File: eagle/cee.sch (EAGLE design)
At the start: 53 parts, among them IC1 IC1, J1 SOLDERJUMPERNC2

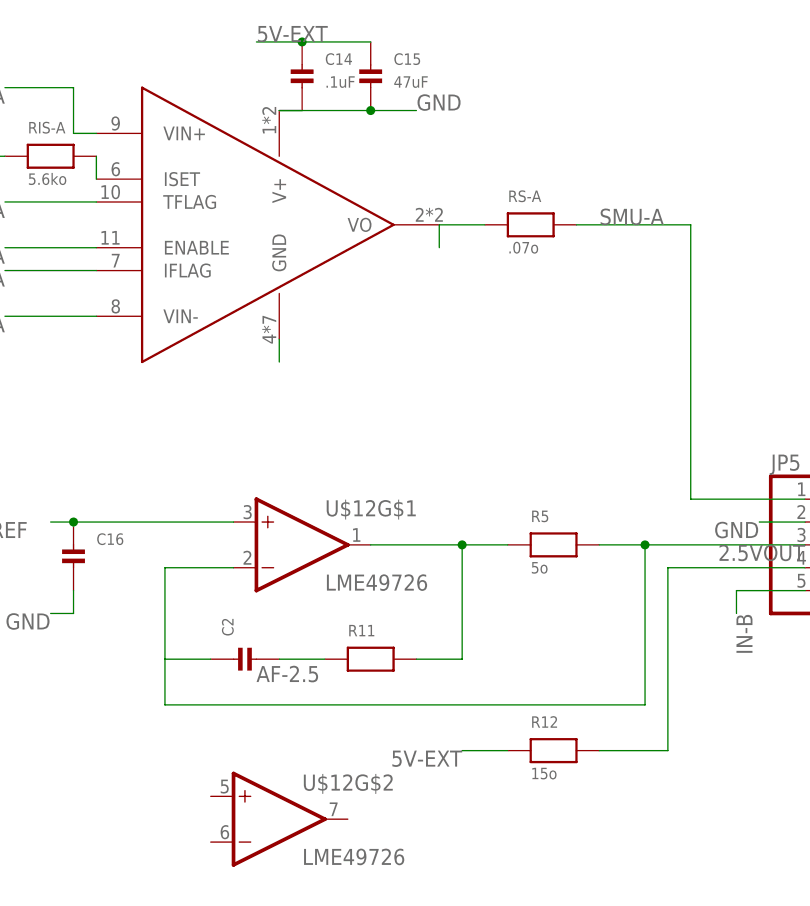
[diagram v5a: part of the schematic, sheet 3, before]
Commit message: Clean up MCP6N11 routing   * Move it to the right place   * Fix 2.5V bypassing   * Fix OPA567 power
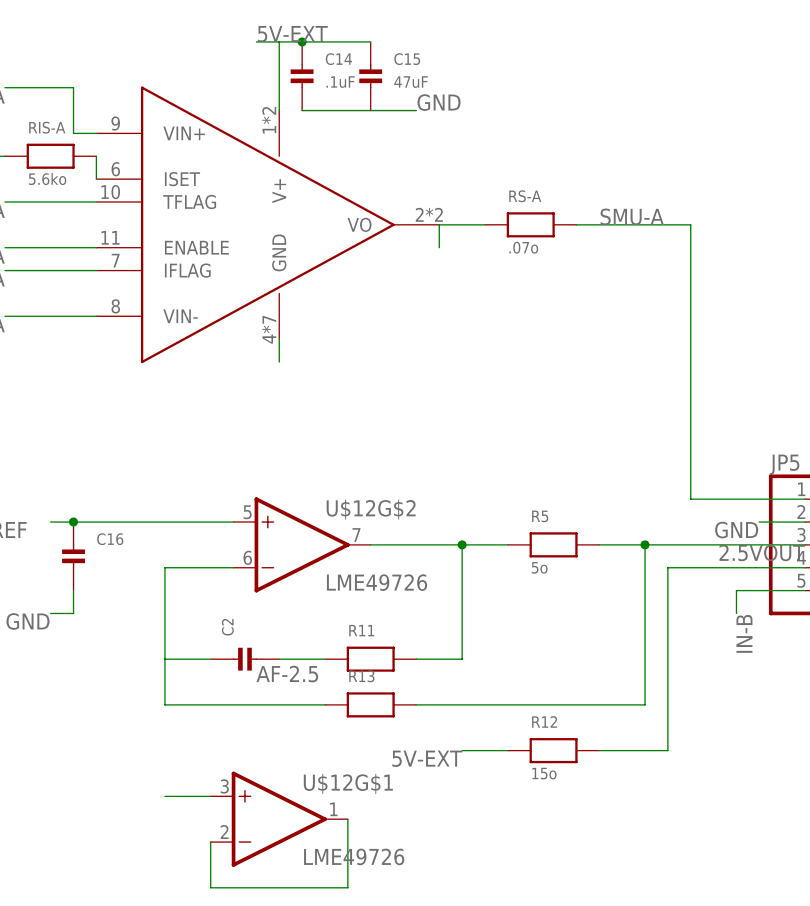
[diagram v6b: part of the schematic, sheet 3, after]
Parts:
- added R13: (no value), nonolith:RESISTOR0603
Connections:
- new net N$13: C2.P$1, R13.1, U$12G$2.-IN
- new net N$15: U$12G$1.-IN, U$12G$1.OUT
- net 2.5VFDBK: now also U$12G$2.OUT; no longer U$12G$1.OUT
- net 2.5VOUT: now also R13.2, U$12G$1.+IN; no longer C2.P$1, U$12G$1.-IN
- net 2.5VREF: now also U$12G$2.+IN; no longer U$12G$1.+IN
- net 5V-EXT: now also OPA-A.V+
- net GND: no longer OPA-A.V+
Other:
- moved on the sheet: U$12G$1, U$12G$2
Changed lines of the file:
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@@
 <?xml version="1.0" encoding="utf-8"?>
 <!DOCTYPE eagle SYSTEM "eagle.dtd">
-<eagle version="6.3">
+<eagle version="6.1">
 <drawing>
 <settings>
@@
 <part name="C2" library="nonolith" deviceset="CAP_CERAMIC" device="0603"/>
 <part name="R12" library="nonolith" deviceset="RESISTOR" device="1206" value="15o"/>
+<part name="R13" library="nonolith" deviceset="RESISTOR" device="0603"/>
 </parts>
 <sheets>
@@
 <instance part="R5" gate="G$1" x="170.18" y="60.96"/>
 <instance part="C12" gate="G$1" x="35.56" y="88.9" rot="R90"/>
-<instance part="U$12" gate="G$1" x="142.24" y="60.96"/>
-<instance part="U$12" gate="G$2" x="139.7" y="30.48"/>
+<instance part="U$12" gate="G$2" x="142.24" y="60.96"/>
+<instance part="U$12" gate="G$1" x="139.7" y="30.48"/>
 <instance part="U$12" gate="G$3" x="106.68" y="38.1"/>
 <instance part="C3" gate="G$1" x="91.44" y="35.56"/>
@@
 <instance part="C2" gate="G$1" x="137.16" y="48.26" rot="R90"/>
 <instance part="R12" gate="G$1" x="170.18" y="38.1"/>
+<instance part="R13" gate="G$1" x="149.86" y="43.18"/>
 </instances>
 <busses>
@@
 </segment>
 <segment>
-<wire x1="139.7" y1="109.22" x2="149.86" y2="109.22" width="0.254" layer="91"/>
 <wire x1="149.86" y1="109.22" x2="154.94" y2="109.22" width="0.254" layer="91"/>
-<junction x="149.86" y="109.22"/>
 <label x="154.94" y="109.22" size="1.778" layer="95"/>
+<pinref part="C15" gate="G$1" pin="P$2"/>
 <pinref part="C14" gate="G$1" pin="P$2"/>
-<pinref part="C15" gate="G$1" pin="P$2"/>
-<pinref part="OPA-A" gate="G$1" pin="V+"/>
-<wire x1="139.7" y1="109.22" x2="142.24" y2="109.22" width="0.1524" layer="91"/>
+<wire x1="142.24" y1="109.22" x2="149.86" y2="109.22" width="0.254" layer="91"/>
 </segment>
 <segment>
@@
 <net name="5V-EXT" class="0">
 <segment>
-<wire x1="137.16" y1="116.84" x2="142.24" y2="116.84" width="0.254" layer="91"/>
+<wire x1="137.16" y1="116.84" x2="139.7" y2="116.84" width="0.254" layer="91"/>
+<wire x1="139.7" y1="116.84" x2="142.24" y2="116.84" width="0.254" layer="91"/>
 <wire x1="142.24" y1="116.84" x2="149.86" y2="116.84" width="0.254" layer="91"/>
 <junction x="142.24" y="116.84"/>
@@
 <pinref part="C14" gate="G$1" pin="P$1"/>
 <pinref part="C15" gate="G$1" pin="P$1"/>
+<pinref part="OPA-A" gate="G$1" pin="V+"/>
+<wire x1="139.7" y1="116.84" x2="139.7" y2="109.22" width="0.254" layer="91"/>
 </segment>
 <segment>
@@
 <net name="2.5VOUT" class="0">
 <segment>
-<pinref part="U$12" gate="G$1" pin="-IN"/>
-<wire x1="134.62" y1="58.42" x2="127" y2="58.42" width="0.254" layer="91"/>
-<wire x1="127" y1="58.42" x2="127" y2="48.26" width="0.254" layer="91"/>
-<wire x1="127" y1="48.26" x2="127" y2="43.18" width="0.254" layer="91"/>
-<wire x1="127" y1="43.18" x2="180.34" y2="43.18" width="0.254" layer="91"/>
+<wire x1="154.94" y1="43.18" x2="180.34" y2="43.18" width="0.254" layer="91"/>
 <wire x1="180.34" y1="43.18" x2="180.34" y2="60.96" width="0.254" layer="91"/>
 <pinref part="R5" gate="G$1" pin="2"/>
@@
 <wire x1="175.26" y1="60.96" x2="180.34" y2="60.96" width="0.254" layer="91"/>
 <label x="198.12" y="60.96" size="1.778" layer="95" rot="R180"/>
-<pinref part="C2" gate="G$1" pin="P$1"/>
 <wire x1="180.34" y1="60.96" x2="198.12" y2="60.96" width="0.254" layer="91"/>
-<wire x1="132.08" y1="48.26" x2="127" y2="48.26" width="0.254" layer="91"/>
 <junction x="180.34" y="60.96"/>
+<pinref part="R13" gate="G$1" pin="2"/>
+</segment>
+<segment>
+<pinref part="U$12" gate="G$1" pin="+IN"/>
+<wire x1="132.08" y1="33.02" x2="127" y2="33.02" width="0.254" layer="91"/>
 </segment>
 </net>
 <net name="2.5VFDBK" class="0">
 <segment>
-<pinref part="U$12" gate="G$1" pin="OUT"/>
+<pinref part="U$12" gate="G$2" pin="OUT"/>
 <wire x1="165.1" y1="60.96" x2="160.02" y2="60.96" width="0.254" layer="91"/>
 <wire x1="160.02" y1="60.96" x2="149.86" y2="60.96" width="0.254" layer="91"/>
@@
 <net name="2.5VREF" class="0">
 <segment>
-<pinref part="U$12" gate="G$1" pin="+IN"/>
+<pinref part="U$12" gate="G$2" pin="+IN"/>
 <wire x1="134.62" y1="63.5" x2="116.84" y2="63.5" width="0.254" layer="91"/>
 <label x="111.76" y="63.5" size="1.778" layer="95" rot="R180"/>
@@
 </segment>
 </net>
+<net name="N$13" class="0">
+<segment>
+<pinref part="R13" gate="G$1" pin="1"/>
+<pinref part="U$12" gate="G$2" pin="-IN"/>
+<wire x1="134.62" y1="58.42" x2="127" y2="58.42" width="0.254" layer="91"/>
+<wire x1="127" y1="58.42" x2="127" y2="48.26" width="0.254" layer="91"/>
+<pinref part="C2" gate="G$1" pin="P$1"/>
+<wire x1="132.08" y1="48.26" x2="127" y2="48.26" width="0.254" layer="91"/>
+<wire x1="127" y1="48.26" x2="127" y2="43.18" width="0.254" layer="91"/>
+<wire x1="127" y1="43.18" x2="144.78" y2="43.18" width="0.254" layer="91"/>
+</segment>
+</net>
+<net name="N$15" class="0">
+<segment>
+<pinref part="U$12" gate="G$1" pin="OUT"/>
+<wire x1="147.32" y1="30.48" x2="147.32" y2="22.86" width="0.254" layer="91"/>
+<pinref part="U$12" gate="G$1" pin="-IN"/>
+<wire x1="147.32" y1="22.86" x2="132.08" y2="22.86" width="0.254" layer="91"/>
+<wire x1="132.08" y1="22.86" x2="132.08" y2="27.94" width="0.254" layer="91"/>
+</segment>
+</net>

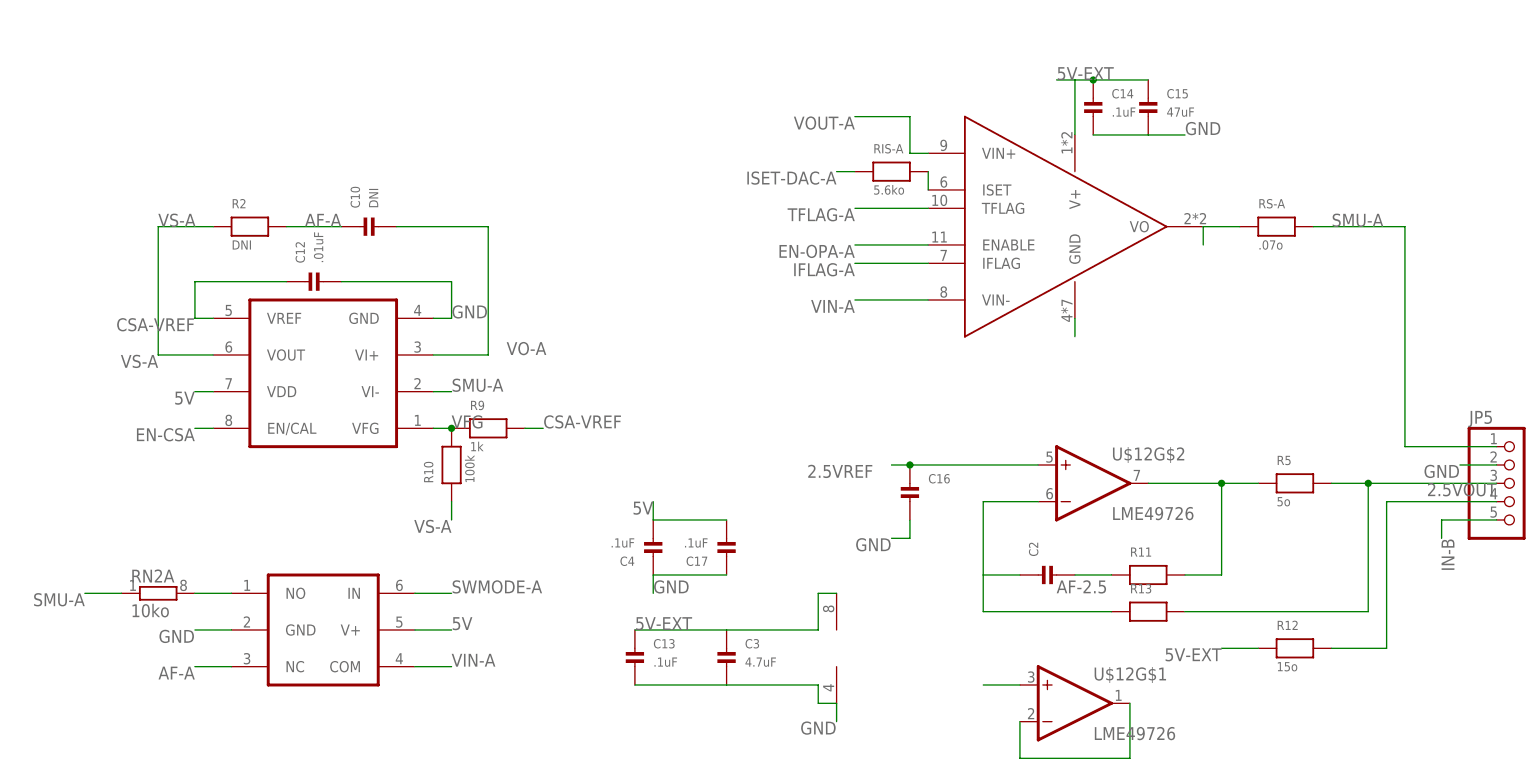
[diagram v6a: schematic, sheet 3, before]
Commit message: Divided 2.5V to ADC gainneg
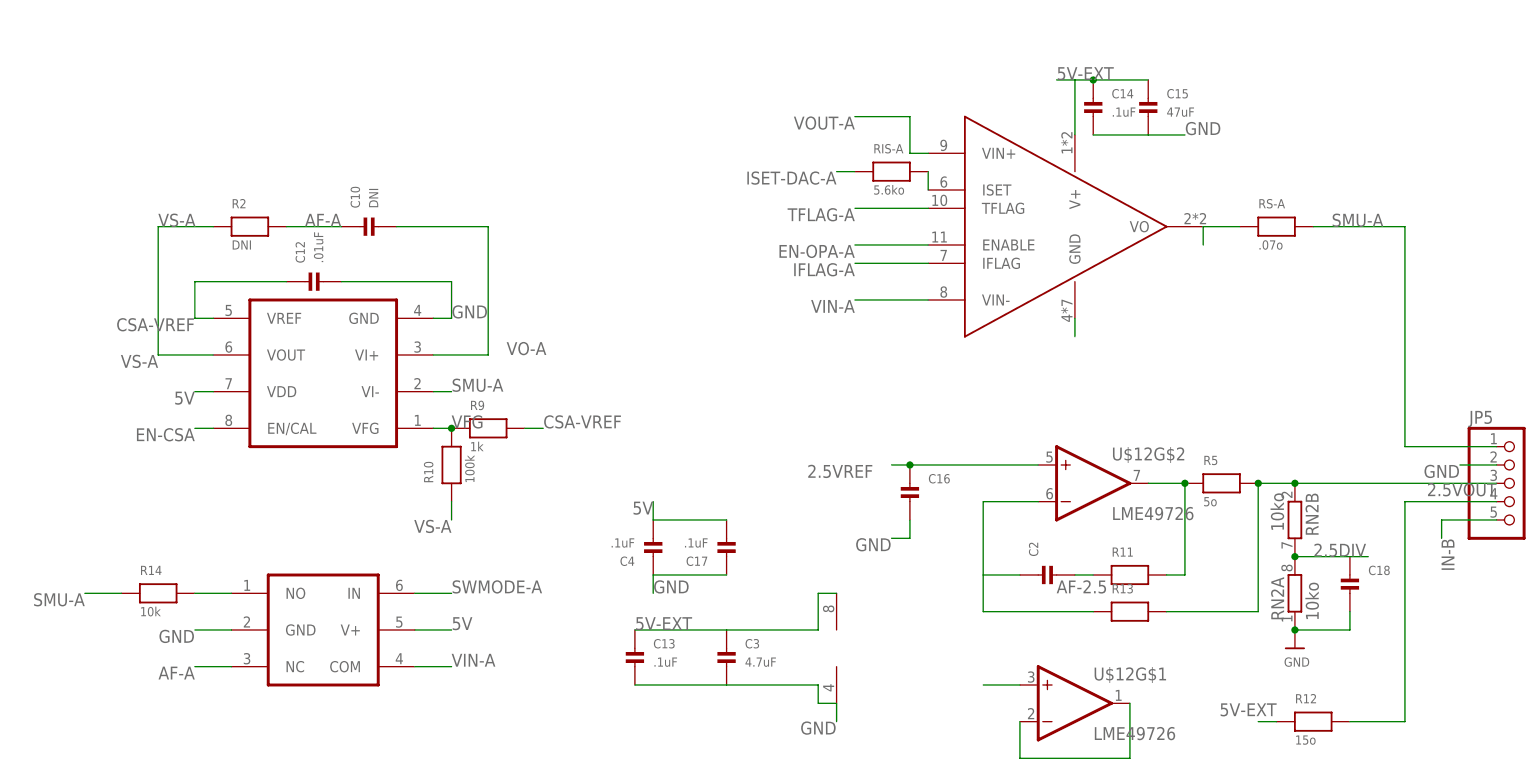
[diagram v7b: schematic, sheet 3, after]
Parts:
- added C18: (no value), nonolith:CAP_CERAMIC0603
- added R14: 10k, nonolith:RESISTOR0603
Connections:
- new net 2.5DIV: C18.P$1, IC1.PA5/ADC5, RN2A.2, RN2B.2
- net 2.5VOUT: now also RN2B.1
- net GND: now also C18.P$2, RN2A.1
- net IN-B: now also RN2D.1; no longer RN2C.1
- net SMU-A: now also R14.1, RN2C.1; no longer RN2A.1, RN2B.1
- net SMUP-A: now also RN2C.2; no longer RN2B.2
- net SMUP-B: now also RN2D.2; no longer RN2C.2
- net SMUP-SW-A: now also R14.2; no longer RN2A.2
- net VOUT-B: now also IC1.PA7/ADC7; no longer IC1.PA5/ADC5
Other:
- moved on the sheet: R11, R12, R13, R5, RN2A, RN2C
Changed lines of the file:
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@@
 <part name="R12" library="nonolith" deviceset="RESISTOR" device="1206" value="15o"/>
 <part name="R13" library="nonolith" deviceset="RESISTOR" device="0603"/>
+<part name="R14" library="nonolith" deviceset="RESISTOR" device="0603" value="10k"/>
+<part name="U$14" library="nonolith" deviceset="GND" device=""/>
+<part name="C18" library="nonolith" deviceset="CAP_CERAMIC" device="0603"/>
 </parts>
 <sheets>
@@
 </segment>
 <segment>
-<wire x1="96.52" y1="17.78" x2="101.6" y2="17.78" width="0.254" layer="91"/>
 <wire x1="96.52" y1="12.7" x2="101.6" y2="12.7" width="0.254" layer="91"/>
-<label x="101.6" y="17.78" size="1.778" layer="95"/>
 <label x="101.6" y="12.7" size="1.778" layer="95"/>
-<pinref part="IC1" gate="G$1" pin="PA5/ADC5"/>
 <pinref part="IC1" gate="G$1" pin="PA3/ADC3"/>
+</segment>
+<segment>
+<pinref part="IC1" gate="G$1" pin="PA7/ADC7"/>
+<wire x1="96.52" y1="22.86" x2="101.6" y2="22.86" width="0.254" layer="91"/>
+<label x="101.6" y="22.86" size="1.778" layer="95"/>
 </segment>
 </net>
@@
 <wire x1="203.2" y1="53.34" x2="195.58" y2="53.34" width="0.254" layer="91"/>
 <label x="195.58" y="53.34" size="1.778" layer="95" rot="R180"/>
+</segment>
+</net>
+<net name="2.5DIV" class="0">
+<segment>
+<pinref part="IC1" gate="G$1" pin="PA5/ADC5"/>
+<wire x1="96.52" y1="17.78" x2="101.6" y2="17.78" width="0.254" layer="91"/>
+<label x="101.6" y="17.78" size="1.778" layer="95"/>
 </segment>
 </net>
@@
 </instance>
 <instance part="OPA-C" gate="G$1" x="22.86" y="58.42" rot="R270"/>
-<instance part="RN2" gate="B" x="5.08" y="45.72" rot="R90"/>
-<instance part="RN2" gate="C" x="5.08" y="17.78" rot="R90"/>
+<instance part="RN2" gate="C" x="5.08" y="45.72" rot="R90"/>
+<instance part="RN2" gate="D" x="5.08" y="17.78" rot="R90"/>
 <instance part="R7" gate="G$1" x="5.08" y="5.08" rot="R90"/>
 </instances>
@@
 <wire x1="5.08" y1="40.64" x2="5.08" y2="38.1" width="0.254" layer="91"/>
 <label x="5.08" y="38.1" size="1.778" layer="95" rot="R270"/>
-<pinref part="RN2" gate="B" pin="1"/>
+<pinref part="RN2" gate="C" pin="1"/>
 </segment>
 </net>
@@
 <wire x1="10.16" y1="22.86" x2="5.08" y2="22.86" width="0.254" layer="91"/>
 <pinref part="OPA-C" gate="A" pin="+IN"/>
-<pinref part="RN2" gate="C" pin="2"/>
+<pinref part="RN2" gate="D" pin="2"/>
 </segment>
 </net>
@@
 <wire x1="10.16" y1="50.8" x2="5.08" y2="50.8" width="0.254" layer="91"/>
 <pinref part="OPA-C" gate="D" pin="+IN"/>
-<pinref part="RN2" gate="B" pin="2"/>
+<pinref part="RN2" gate="C" pin="2"/>
 </segment>
 </net>
@@
 <net name="IN-B" class="0">
 <segment>
-<pinref part="RN2" gate="C" pin="1"/>
+<pinref part="RN2" gate="D" pin="1"/>
 <wire x1="5.08" y1="12.7" x2="5.08" y2="10.16" width="0.254" layer="91"/>
 <label x="5.08" y="10.16" size="1.778" layer="95"/>
@@
 <instance part="R2" gate="G$1" x="25.4" y="96.52"/>
 <instance part="C10" gate="G$1" x="43.18" y="96.52" rot="R90"/>
-<instance part="RN2" gate="A" x="12.7" y="45.72"/>
 <instance part="JP5" gate="A" x="200.66" y="60.96"/>
-<instance part="R5" gate="G$1" x="170.18" y="60.96"/>
+<instance part="R5" gate="G$1" x="160.02" y="60.96"/>
 <instance part="C12" gate="G$1" x="35.56" y="88.9" rot="R90"/>
 <instance part="U$12" gate="G$2" x="142.24" y="60.96"/>
@@
 <instance part="R9" gate="G$1" x="58.42" y="68.58"/>
 <instance part="R10" gate="G$1" x="53.34" y="63.5" rot="R90"/>
-<instance part="R11" gate="G$1" x="149.86" y="48.26"/>
+<instance part="R11" gate="G$1" x="147.32" y="48.26"/>
 <instance part="C2" gate="G$1" x="137.16" y="48.26" rot="R90"/>
-<instance part="R12" gate="G$1" x="170.18" y="38.1"/>
-<instance part="R13" gate="G$1" x="149.86" y="43.18"/>
+<instance part="R12" gate="G$1" x="172.72" y="27.94"/>
+<instance part="R13" gate="G$1" x="147.32" y="43.18"/>
+<instance part="R14" gate="G$1" x="12.7" y="45.72"/>
+<instance part="U$14" gate="G$1" x="170.18" y="38.1"/>
+<instance part="C18" gate="G$1" x="177.8" y="45.72"/>
+<instance part="RN2" gate="A" x="170.18" y="45.72" rot="R90"/>
+<instance part="RN2" gate="B" x="170.18" y="55.88" rot="R270"/>
 </instances>
 <busses>
@@
 <wire x1="139.7" y1="83.82" x2="139.7" y2="81.28" width="0.254" layer="91"/>
 </segment>
+<segment>
+<pinref part="U$14" gate="G$1" pin="GND"/>
+<pinref part="C18" gate="G$1" pin="P$2"/>
+<wire x1="170.18" y1="40.64" x2="177.8" y2="40.64" width="0.254" layer="91"/>
+<wire x1="177.8" y1="40.64" x2="177.8" y2="43.18" width="0.254" layer="91"/>
+<pinref part="RN2" gate="A" pin="1"/>
+<junction x="170.18" y="40.64"/>
+</segment>
 </net>
 <net name="VOUT-A" class="0">
@@
 <wire x1="7.62" y1="45.72" x2="2.54" y2="45.72" width="0.254" layer="91"/>
 <label x="2.54" y="45.72" size="1.778" layer="95" rot="R180"/>
-<pinref part="RN2" gate="A" pin="1"/>
+<pinref part="R14" gate="G$1" pin="1"/>
 </segment>
 <segment>
@@
 <segment>
 <pinref part="R12" gate="G$1" pin="1"/>
-<wire x1="165.1" y1="38.1" x2="160.02" y2="38.1" width="0.254" layer="91"/>
-<label x="160.02" y="38.1" size="1.778" layer="95" rot="R180"/>
+<wire x1="167.64" y1="27.94" x2="165.1" y2="27.94" width="0.254" layer="91"/>
+<label x="167.64" y="30.48" size="1.778" layer="95" rot="R180"/>
 </segment>
 </net>
@@
 <wire x1="22.86" y1="45.72" x2="17.78" y2="45.72" width="0.254" layer="91"/>
 <pinref part="SW-A" gate="G$1" pin="NO"/>
-<pinref part="RN2" gate="A" pin="2"/>
+<pinref part="R14" gate="G$1" pin="2"/>
 </segment>
 </net>
@@
 <net name="2.5VOUT" class="0">
 <segment>
-<wire x1="154.94" y1="43.18" x2="180.34" y2="43.18" width="0.254" layer="91"/>
-<wire x1="180.34" y1="43.18" x2="180.34" y2="60.96" width="0.254" layer="91"/>
+<wire x1="152.4" y1="43.18" x2="165.1" y2="43.18" width="0.254" layer="91"/>
+<wire x1="165.1" y1="43.18" x2="165.1" y2="60.96" width="0.254" layer="91"/>
 <pinref part="R5" gate="G$1" pin="2"/>
 <pinref part="JP5" gate="A" pin="3"/>
-<wire x1="175.26" y1="60.96" x2="180.34" y2="60.96" width="0.254" layer="91"/>
 <label x="198.12" y="60.96" size="1.778" layer="95" rot="R180"/>
-<wire x1="180.34" y1="60.96" x2="198.12" y2="60.96" width="0.254" layer="91"/>
-<junction x="180.34" y="60.96"/>
+<wire x1="165.1" y1="60.96" x2="170.18" y2="60.96" width="0.254" layer="91"/>
+<junction x="165.1" y="60.96"/>
 <pinref part="R13" gate="G$1" pin="2"/>
+<wire x1="170.18" y1="60.96" x2="198.12" y2="60.96" width="0.254" layer="91"/>
+<junction x="170.18" y="60.96"/>
+<pinref part="RN2" gate="B" pin="1"/>
 </segment>
 <segment>
@@
 <segment>
 <pinref part="U$12" gate="G$2" pin="OUT"/>
-<wire x1="165.1" y1="60.96" x2="160.02" y2="60.96" width="0.254" layer="91"/>
-<wire x1="160.02" y1="60.96" x2="149.86" y2="60.96" width="0.254" layer="91"/>
+<wire x1="154.94" y1="60.96" x2="149.86" y2="60.96" width="0.254" layer="91"/>
 <pinref part="R5" gate="G$1" pin="1"/>
 <pinref part="R11" gate="G$1" pin="2"/>
-<wire x1="154.94" y1="48.26" x2="160.02" y2="48.26" width="0.254" layer="91"/>
-<wire x1="160.02" y1="48.26" x2="160.02" y2="60.96" width="0.254" layer="91"/>
-<junction x="160.02" y="60.96"/>
+<wire x1="152.4" y1="48.26" x2="154.94" y2="48.26" width="0.254" layer="91"/>
+<wire x1="154.94" y1="48.26" x2="154.94" y2="60.96" width="0.254" layer="91"/>
+<junction x="154.94" y="60.96"/>
 </segment>
 </net>
@@
 <pinref part="R11" gate="G$1" pin="1"/>
 <pinref part="C2" gate="G$1" pin="P$2"/>
-<wire x1="144.78" y1="48.26" x2="139.7" y2="48.26" width="0.254" layer="91"/>
+<wire x1="142.24" y1="48.26" x2="139.7" y2="48.26" width="0.254" layer="91"/>
 <label x="137.16" y="45.72" size="1.778" layer="95"/>
 </segment>
@@
 <segment>
 <pinref part="JP5" gate="A" pin="4"/>
-<wire x1="198.12" y1="58.42" x2="182.88" y2="58.42" width="0.254" layer="91"/>
-<wire x1="182.88" y1="58.42" x2="182.88" y2="38.1" width="0.254" layer="91"/>
-<wire x1="182.88" y1="38.1" x2="175.26" y2="38.1" width="0.254" layer="91"/>
+<wire x1="198.12" y1="58.42" x2="185.42" y2="58.42" width="0.254" layer="91"/>
+<wire x1="185.42" y1="58.42" x2="185.42" y2="27.94" width="0.254" layer="91"/>
+<wire x1="185.42" y1="27.94" x2="177.8" y2="27.94" width="0.254" layer="91"/>
 <pinref part="R12" gate="G$1" pin="2"/>
 </segment>
@@
 <wire x1="132.08" y1="48.26" x2="127" y2="48.26" width="0.254" layer="91"/>
 <wire x1="127" y1="48.26" x2="127" y2="43.18" width="0.254" layer="91"/>
-<wire x1="127" y1="43.18" x2="144.78" y2="43.18" width="0.254" layer="91"/>
+<wire x1="127" y1="43.18" x2="142.24" y2="43.18" width="0.254" layer="91"/>
 </segment>
 </net>
@@
 </segment>
 </net>
+<net name="2.5DIV" class="0">
+<segment>
+<wire x1="170.18" y1="50.8" x2="177.8" y2="50.8" width="0.254" layer="91"/>
+<pinref part="C18" gate="G$1" pin="P$1"/>
+<pinref part="RN2" gate="A" pin="2"/>
+<pinref part="RN2" gate="B" pin="2"/>
+<junction x="170.18" y="50.8"/>
+<wire x1="177.8" y1="50.8" x2="180.34" y2="50.8" width="0.254" layer="91"/>
+<label x="172.72" y="50.8" size="1.778" layer="95"/>
+</segment>
+</net>
